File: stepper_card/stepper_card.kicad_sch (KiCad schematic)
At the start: 25 parts, among them J1 Bus_PCI_Express_x1, J2 Conn_01x04, J3 Conn_01x06_Pin, J4 Conn_01x01_Pin, J5 Conn_01x01_Pin, J6 Conn_01x01_Pin, J7 Conn_01x01_Pin, J8 Conn_01x01_Pin, SW1 SW_DIP_x04, U1 DRV8825PWPR_Stepper_Driver

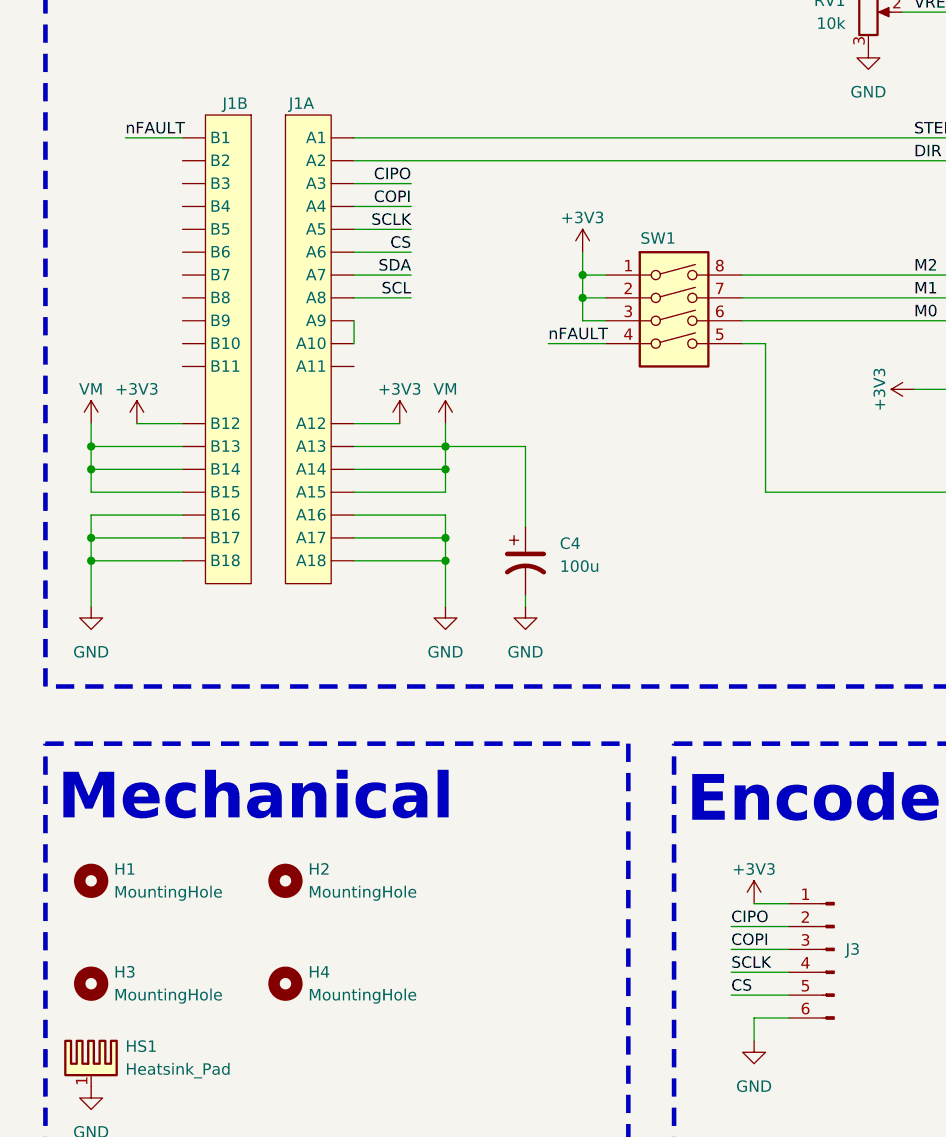
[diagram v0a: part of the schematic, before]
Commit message: changed pinout
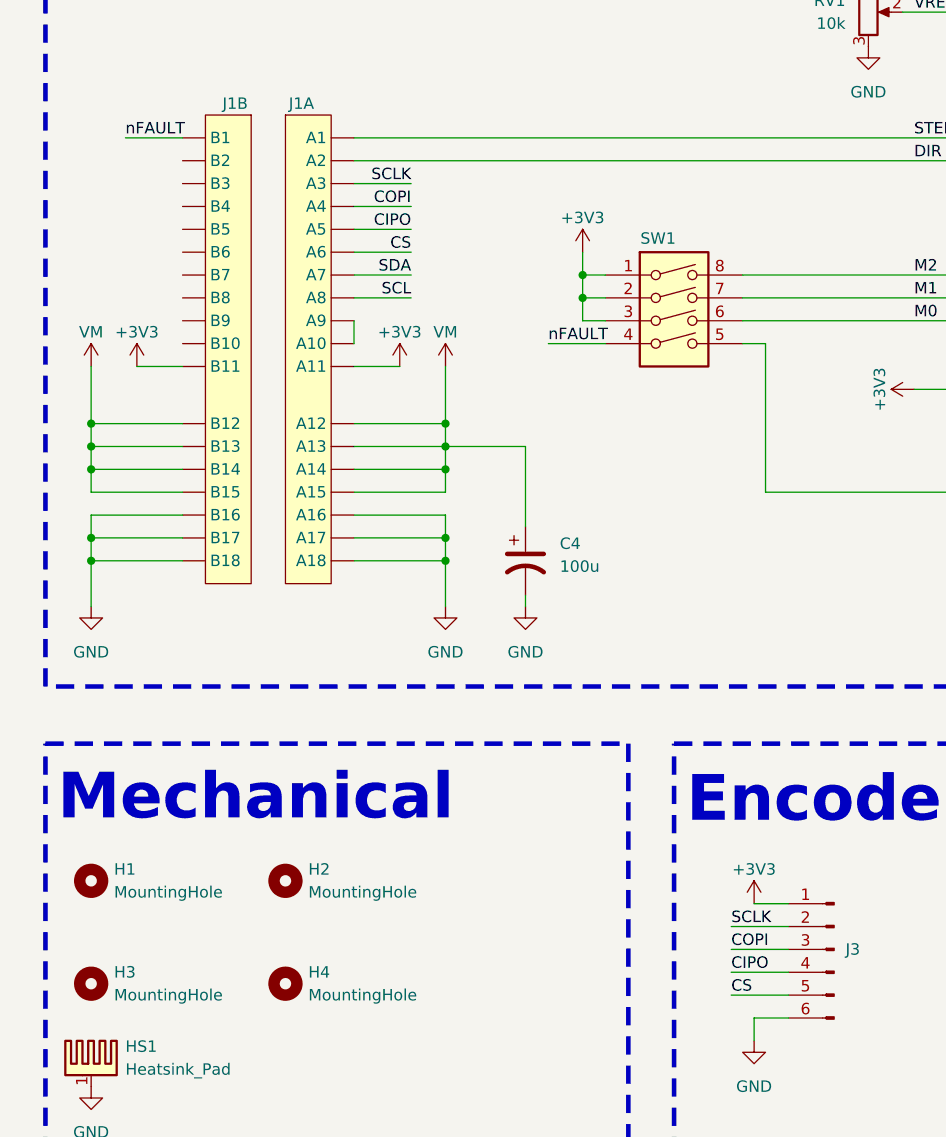
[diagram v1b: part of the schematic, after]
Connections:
- net +3V3: now also J1.A11, J1.B11; no longer J1.A12, J1.B12
- net CIPO: now also J1.A5, J3.4 (Pin_4); no longer J1.A3, J3.2 (Pin_2)
- net SCLK: now also J1.A3, J3.2 (Pin_2); no longer J1.A5, J3.4 (Pin_4)
- net VM: now also J1.A12, J1.B12
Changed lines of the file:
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@@
 	)
 	(junction
+		(at 60.96 78.74)
+		(diameter 0)
+		(color 0 0 0 0)
+	)
+	(junction
 		(at 182.88 38.1)
 		(diameter 0)
@@
 	)
 	(junction
+		(at 21.59 78.74)
+		(diameter 0)
+		(color 0 0 0 0)
+	)
+	(junction
 		(at 118.11 74.93)
 		(diameter 0)
@@
 	(wire
 		(pts
+			(xy 21.59 78.74) (xy 21.59 81.28)
+		)
+		(stroke
+			(width 0)
+			(type default)
+		)
+	)
+	(wire
+		(pts
 			(xy 195.58 36.83) (xy 195.58 38.1)
 		)
@@
 	(wire
 		(pts
+			(xy 26.67 72.39) (xy 31.75 72.39)
+		)
+		(stroke
+			(width 0)
+			(type default)
+		)
+	)
+	(wire
+		(pts
 			(xy 182.88 36.83) (xy 182.88 38.1)
 		)
@@
 	(wire
 		(pts
+			(xy 21.59 78.74) (xy 31.75 78.74)
+		)
+		(stroke
+			(width 0)
+			(type default)
+		)
+	)
+	(wire
+		(pts
 			(xy 76.2 64.77) (xy 78.74 64.77)
 		)
@@
 	(wire
 		(pts
-			(xy 50.8 83.82) (xy 60.96 83.82)
+			(xy 50.8 78.74) (xy 60.96 78.74)
 		)
 		(stroke
@@
 	(wire
 		(pts
-			(xy 50.8 78.74) (xy 55.88 78.74)
+			(xy 50.8 83.82) (xy 60.96 83.82)
 		)
 		(stroke
@@
 	(wire
 		(pts
-			(xy 21.59 78.74) (xy 21.59 81.28)
+			(xy 21.59 72.39) (xy 21.59 78.74)
 		)
 		(stroke
@@
 	(wire
 		(pts
+			(xy 60.96 78.74) (xy 60.96 81.28)
+		)
+		(stroke
+			(width 0)
+			(type default)
+		)
+	)
+	(wire
+		(pts
 			(xy 93.98 62.23) (xy 120.65 62.23)
 		)
@@
 	(wire
 		(pts
-			(xy 165.1 77.47) (xy 147.32 77.47)
+			(xy 50.8 72.39) (xy 55.88 72.39)
 		)
 		(stroke
@@
 	(wire
 		(pts
-			(xy 21.59 86.36) (xy 21.59 83.82)
+			(xy 165.1 77.47) (xy 147.32 77.47)
 		)
 		(stroke
@@
 	(wire
 		(pts
-			(xy 60.96 91.44) (xy 60.96 93.98)
+			(xy 21.59 86.36) (xy 21.59 83.82)
 		)
 		(stroke
@@
 	(wire
 		(pts
-			(xy 60.96 78.74) (xy 60.96 81.28)
+			(xy 60.96 91.44) (xy 60.96 93.98)
 		)
 		(stroke
@@
 	(wire
 		(pts
-			(xy 171.45 38.1) (xy 171.45 36.83)
+			(xy 60.96 72.39) (xy 60.96 78.74)
 		)
 		(stroke
@@
 	(wire
 		(pts
-			(xy 50.8 88.9) (xy 60.96 88.9)
+			(xy 171.45 38.1) (xy 171.45 36.83)
 		)
 		(stroke
@@
 	(wire
 		(pts
-			(xy 119.38 35.56) (xy 119.38 33.02)
+			(xy 50.8 88.9) (xy 60.96 88.9)
 		)
 		(stroke
@@
 	(wire
 		(pts
-			(xy 21.59 83.82) (xy 21.59 81.28)
+			(xy 119.38 35.56) (xy 119.38 33.02)
 		)
 		(stroke
@@
 	(wire
 		(pts
-			(xy 26.67 78.74) (xy 31.75 78.74)
+			(xy 21.59 83.82) (xy 21.59 81.28)
 		)
 		(stroke
@@
 		)
 	)
+	(label "CIPO"
+		(at 92.71 139.7 0)
+		(effects
+			(font
+				(size 1.27 1.27)
+			)
+			(justify left bottom)
+		)
+	)
+	(label "SCLK"
+		(at 92.71 134.62 0)
+		(effects
+			(font
+				(size 1.27 1.27)
+			)
+			(justify left bottom)
+		)
+	)
 	(label "SDA"
 		(at 57.15 62.23 180)
@@
 		)
 	)
-	(label "SCLK"
-		(at 57.15 57.15 180)
-		(effects
-			(font
-				(size 1.27 1.27)
-			)
-			(justify right bottom)
-		)
-	)
 	(label "GND"
 		(at 191.77 133.35 0)
@@
 		)
 	)
-	(label "CIPO"
-		(at 57.15 52.07 180)
-		(effects
-			(font
-				(size 1.27 1.27)
-			)
-			(justify right bottom)
-		)
-	)
 	(label "B1"
 		(at 149.86 64.77 0)
@@
 	)
 	(label "CIPO"
-		(at 92.71 134.62 0)
+		(at 57.15 57.15 180)
 		(effects
 			(font
 				(size 1.27 1.27)
 			)
-			(justify left bottom)
+			(justify right bottom)
 		)
 	)
@@
 		)
 	)
+	(label "SCLK"
+		(at 57.15 52.07 180)
+		(effects
+			(font
+				(size 1.27 1.27)
+			)
+			(justify right bottom)
+		)
+	)
 	(label "B2"
 		(at 149.86 62.23 0)
@@
 		)
 	)
-	(label "SCLK"
-		(at 92.71 139.7 0)
-		(effects
-			(font
-				(size 1.27 1.27)
-			)
-			(justify left bottom)
-		)
-	)
 	(label "SCL"
 		(at 57.15 64.77 180)
@@
 	(symbol
 		(lib_id "power:+3V3")
-		(at 26.67 78.74 0)
+		(at 26.67 72.39 0)
 		(unit 1)
 		(exclude_from_sim no)
@@
 		(dnp no)
 		(property "Reference" "#PWR011"
-			(at 26.67 82.55 0)
+			(at 26.67 76.2 0)
 			(effects
 				(font
@@
 		)
 		(property "Value" "+3V3"
-			(at 26.67 74.93 0)
+			(at 26.67 68.58 0)
 			(effects
 				(font
@@
 		)
 		(property "Footprint" ""
-			(at 26.67 78.74 0)
+			(at 26.67 72.39 0)
 			(effects
 				(font
@@
 		)
 		(property "Datasheet" ""
-			(at 26.67 78.74 0)
+			(at 26.67 72.39 0)
 			(effects
 				(font
@@
 		)
 		(property "Description" "Power symbol creates a global label with name \"+3V3\""
-			(at 26.67 78.74 0)
+			(at 26.67 72.39 0)
 			(effects
 				(font
@@
 	(symbol
 		(lib_id "power:+9V")
-		(at 60.96 78.74 0)
+		(at 60.96 72.39 0)
 		(unit 1)
 		(exclude_from_sim no)
@@
 		(dnp no)
 		(property "Reference" "#PWR07"
-			(at 60.96 82.55 0)
+			(at 60.96 76.2 0)
 			(effects
 				(font
@@
 		)
 		(property "Value" "VM"
-			(at 60.96 74.93 0)
+			(at 60.96 68.58 0)
 			(effects
 				(font
@@
 		)
 		(property "Footprint" ""
-			(at 60.96 78.74 0)
+			(at 60.96 72.39 0)
 			(effects
 				(font
@@
 		)
 		(property "Datasheet" ""
-			(at 60.96 78.74 0)
+			(at 60.96 72.39 0)
 			(effects
 				(font
@@
 		)
 		(property "Description" "Power symbol creates a global label with name \"+9V\""
-			(at 60.96 78.74 0)
+			(at 60.96 72.39 0)
 			(effects
 				(font
@@
 	(symbol
 		(lib_id "power:+9V")
-		(at 21.59 78.74 0)
+		(at 21.59 72.39 0)
 		(unit 1)
 		(exclude_from_sim no)
@@
 		(dnp no)
 		(property "Reference" "#PWR08"
-			(at 21.59 82.55 0)
+			(at 21.59 76.2 0)
 			(effects
 				(font
@@
 		)
 		(property "Value" "VM"
-			(at 21.59 74.93 0)
+			(at 21.59 68.58 0)
 			(effects
 				(font
@@
 		)
 		(property "Footprint" ""
-			(at 21.59 78.74 0)
+			(at 21.59 72.39 0)
 			(effects
 				(font
@@
 		)
 		(property "Datasheet" ""
-			(at 21.59 78.74 0)
+			(at 21.59 72.39 0)
 			(effects
 				(font
@@
 		)
 		(property "Description" "Power symbol creates a global label with name \"+9V\""
-			(at 21.59 78.74 0)
+			(at 21.59 72.39 0)
 			(effects
 				(font
@@
 	(symbol
 		(lib_id "power:+3V3")
-		(at 55.88 78.74 0)
+		(at 55.88 72.39 0)
 		(unit 1)
 		(exclude_from_sim no)
@@
 		(dnp no)
 		(property "Reference" "#PWR012"
-			(at 55.88 82.55 0)
+			(at 55.88 76.2 0)
 			(effects
 				(font
@@
 		)
 		(property "Value" "+3V3"
-			(at 55.88 74.93 0)
+			(at 55.88 68.58 0)
 			(effects
 				(font
@@
 		)
 		(property "Footprint" ""
-			(at 55.88 78.74 0)
+			(at 55.88 72.39 0)
 			(effects
 				(font
@@
 		)
 		(property "Datasheet" ""
-			(at 55.88 78.74 0)
+			(at 55.88 72.39 0)
 			(effects
 				(font
@@
 		)
 		(property "Description" "Power symbol creates a global label with name \"+3V3\""
-			(at 55.88 78.74 0)
+			(at 55.88 72.39 0)
 			(effects
 				(font
